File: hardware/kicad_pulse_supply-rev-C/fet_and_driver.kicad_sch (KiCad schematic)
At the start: 52 parts, among them J2 SIG_EXT, Q3 GAN7R0-150LBE, U4 MAX4378, U5 UCC27611DRVT, U6 MCP1703T-5002E/MB

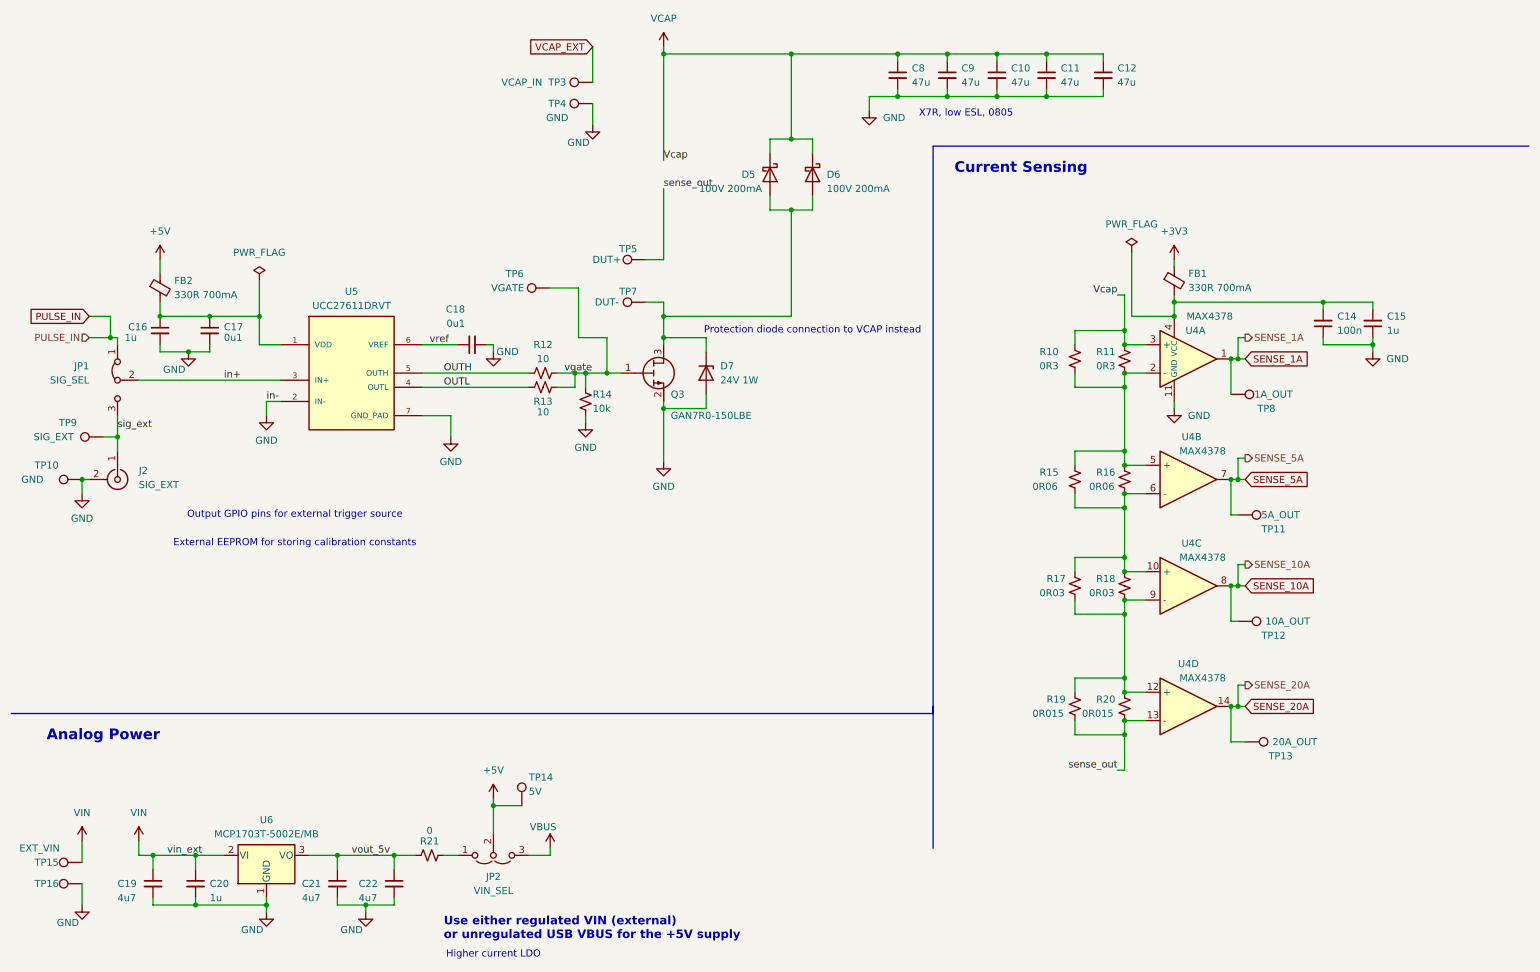
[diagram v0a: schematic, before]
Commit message: hardware breakout boards added, pcb rev-c began
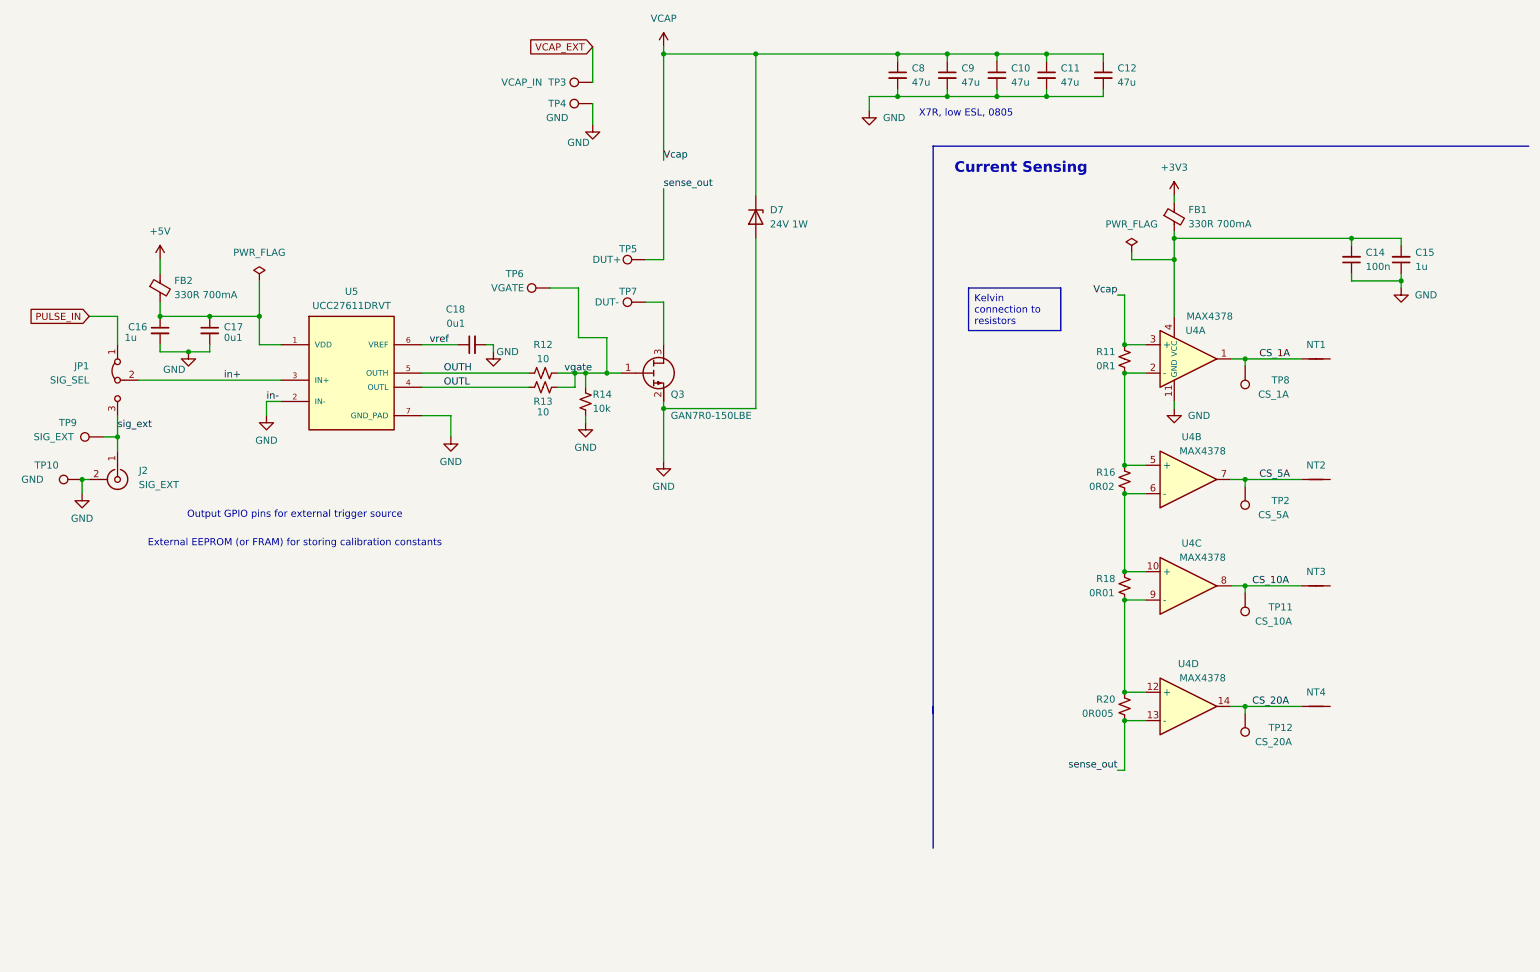
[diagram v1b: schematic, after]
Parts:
- removed C19, C21, C22: 4u7, Capacitor_SMD:C_0805_2012Metric_Pad1.18x1.45mm_HandSolder, symbol Device:C_Small
- removed C20: 1u, Capacitor_SMD:C_0603_1608Metric_Pad1.08x0.95mm_HandSolder, symbol Device:C_Small
- removed D5, D6: 100V 200mA, Diode_SMD:D_SOD-323F, symbol Device:D_Schottky
- removed JP2: VIN_SEL, Connector_PinHeader_2.54mm:PinHeader_1x03_P2.54mm_Vertical, symbol Jumper:Jumper_3_Open
- removed R10: 0R3, Resistor_SMD:R_2010_5025Metric_Pad1.40x2.65mm_HandSolder, symbol Device:R_Small_US
- removed R15: 0R06, Resistor_SMD:R_2010_5025Metric_Pad1.40x2.65mm_HandSolder, symbol Device:R_Small_US
- removed R17: 0R03, Resistor_SMD:R_1206_3216Metric_Pad1.30x1.75mm_HandSolder, symbol Device:R_Small_US
- removed R19: 0R015, Resistor_SMD:R_1206_3216Metric_Pad1.30x1.75mm_HandSolder, symbol Device:R_Small_US
- removed R21: 0, Resistor_SMD:R_0603_1608Metric_Pad0.98x0.95mm_HandSolder, symbol Device:R_Small_US
- removed TP13: 20A_OUT, DW_Library:Keystone-1502-2, symbol Connector:TestPoint
- removed TP14: 5V, DW_Library:Keystone-1502-2, symbol Connector:TestPoint
- removed TP15: EXT_VIN, DW_Library:Keystone-1502-2, symbol Connector:TestPoint
- removed TP16: GND, DW_Library:Keystone-1502-2, symbol Connector:TestPoint
- removed U6: MCP1703T-5002E/MB, Package_TO_SOT_SMD:SOT-89-3, symbol Regulator_Linear:MCP1703Ax-500xxMB
- added NT1, NT2, NT3, NT4: NetTie_2, symbol Device:NetTie_2
- added TP2: CS_5A, DW_Library:Keystone-1502-2, symbol Connector:TestPoint
- R11: value 0R3 -> 0R1; footprint Resistor_SMD:R_2010_5025Metric_Pad1.40x2.65mm_HandSolder -> Resistor_SMD:R_2512_6332Metric
- R16: value 0R06 -> 0R02
- R18: value 0R03 -> 0R01; footprint Resistor_SMD:R_1206_3216Metric_Pad1.30x1.75mm_HandSolder -> Resistor_SMD:R_2512_6332Metric
- R20: value 0R015 -> 0R005; footprint Resistor_SMD:R_1206_3216Metric_Pad1.30x1.75mm_HandSolder -> Resistor_SMD:R_Shunt_Ohmite_LVK25
- TP11: value 5A_OUT -> CS_10A
- TP12: value 10A_OUT -> CS_20A
- TP8: value 1A_OUT -> CS_1A
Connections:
- net VCAP: now also D7.1 (K)
- net at Q3.3 (D), TP7.1: no longer D7.1 (K)
- net SENSE_10A renamed CS_10A
- net CS_10A: now also TP11.1, NT3.1; no longer TP12.1
- net SENSE_1A renamed CS_1A
- net CS_1A: now also NT1.1
- net SENSE_20A renamed CS_20A
- net CS_20A: now also TP12.1, NT4.1
- net SENSE_5A renamed CS_5A
- net CS_5A: now also NT2.1, TP2.1; no longer TP11.1
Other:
- note added: "External EEPROM (or FRAM) for storing calibration constants"
- note removed: "Analog Power"
- note removed: "External EEPROM for storing calibration constants"
- note removed: "Higher current LDO"
- note removed: "Protection diode connection to VCAP instead"
- note removed: "Use either regulated VIN (external) or unregulated USB VBUS for the +5V supply"
- moved on the sheet: C14, C15, D7, FB1, TP8

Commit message: Rev C pcb complete, last commit before branching firmware for new board
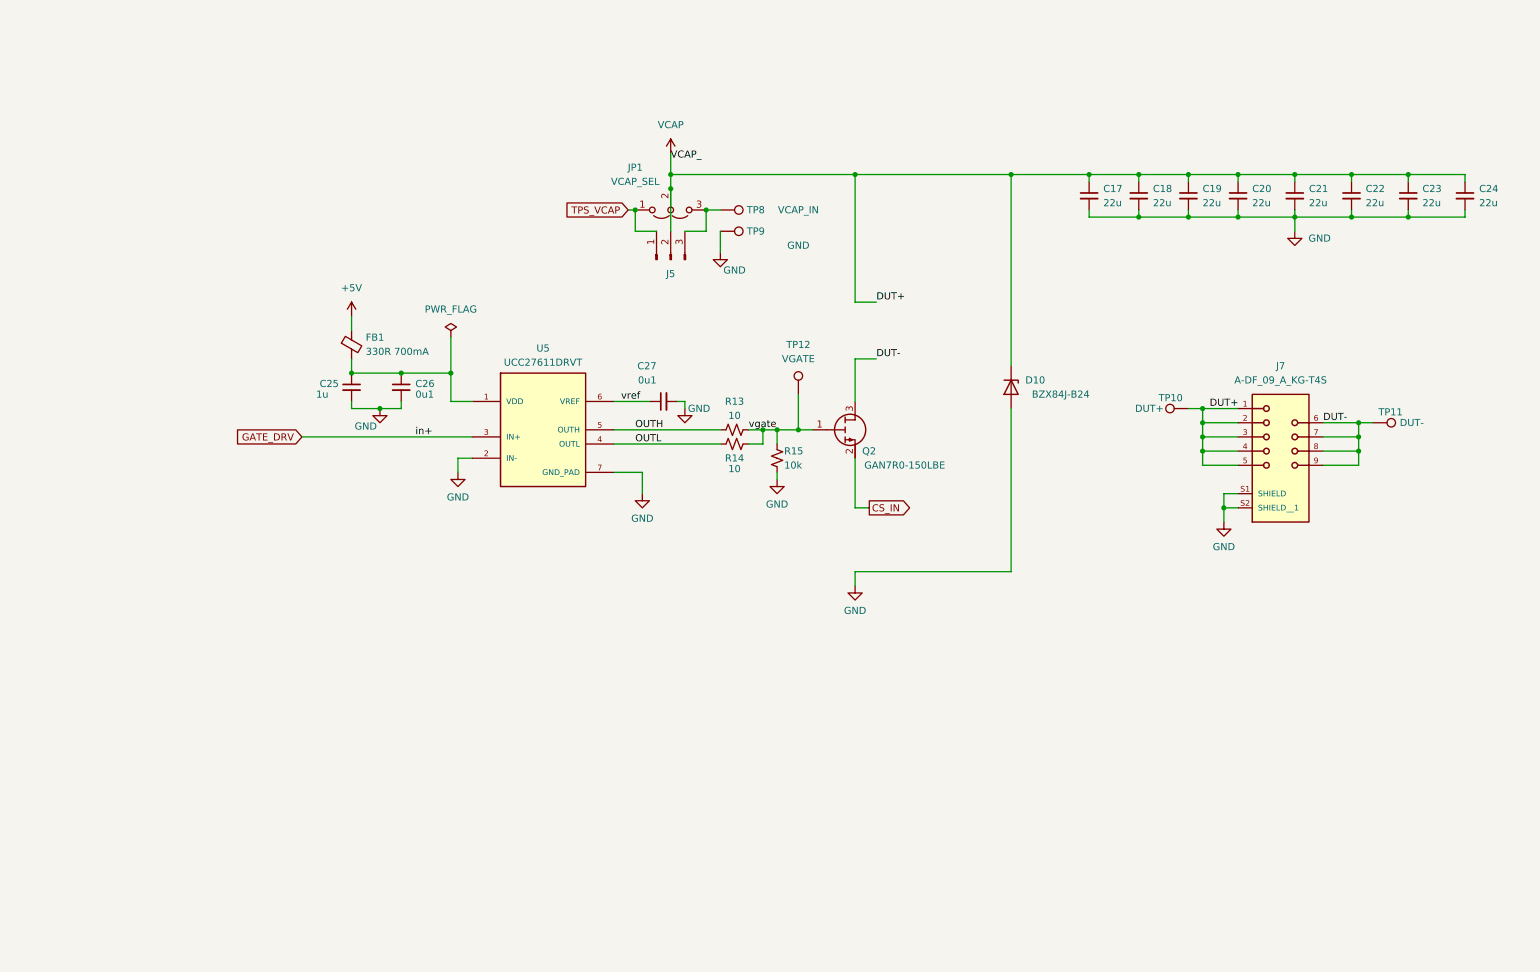
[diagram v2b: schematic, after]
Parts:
- removed C14: 100n, Capacitor_SMD:C_0603_1608Metric_Pad1.08x0.95mm_HandSolder, symbol Device:C_Small
- removed C15: 1u, Capacitor_SMD:C_0603_1608Metric_Pad1.08x0.95mm_HandSolder, symbol Device:C_Small
- removed FB1: 330R 700mA, Capacitor_SMD:C_0402_1005Metric_Pad0.74x0.62mm_HandSolder, symbol Device:FerriteBead_Small
- removed J2: SIG_EXT, DW_Library:BNC_Molex_0731375003, symbol Connector:Conn_Coaxial
- removed JP1: SIG_SEL, Connector_PinHeader_2.54mm:PinHeader_1x03_P2.54mm_Vertical, symbol Jumper:Jumper_3_Bridged12
- removed NT1, NT2, NT3, NT4: NetTie_2, symbol Device:NetTie_2
- removed R11: 0R1, Resistor_SMD:R_2512_6332Metric, symbol Device:R_Small_US
- removed R16: 0R02, Resistor_SMD:R_2010_5025Metric_Pad1.40x2.65mm_HandSolder, symbol Device:R_Small_US
- removed R18: 0R01, Resistor_SMD:R_2512_6332Metric, symbol Device:R_Small_US
- removed R20: 0R005, Resistor_SMD:R_Shunt_Ohmite_LVK25, symbol Device:R_Small_US
- removed TP10: GND, DW_Library:Keystone-1502-2, symbol Connector:TestPoint
- removed TP11: CS_10A, DW_Library:Keystone-1502-2, symbol Connector:TestPoint
- removed TP12: CS_20A, DW_Library:Keystone-1502-2, symbol Connector:TestPoint
- removed TP2: CS_5A, DW_Library:Keystone-1502-2, symbol Connector:TestPoint
- removed TP8: CS_1A, DW_Library:Keystone-1502-2, symbol Connector:TestPoint
- removed TP9: SIG_EXT, DW_Library:Keystone-1502-2, symbol Connector:TestPoint
- removed U4: MAX4378, Package_SO:TSSOP-14_4.4x5mm_P0.65mm, symbol DW_custom_symbols:MAX4378
- added C22, C23, C24: 22u, Capacitor_SMD:C_0805_2012Metric, symbol Device:C_Small
- added J5: Conn_01x03_Pin, Connector_PinHeader_2.54mm:PinHeader_1x03_P2.54mm_Vertical, symbol Connector:Conn_01x03_Pin
- added J7: A-DF_09_A_KG-T4S, DW_Library:ASSMANN_A-DF_09_A_KG-T4S, symbol DW_Library:A-DF_09_A_KG-T4S
- added JP1: VCAP_SEL, DW_Library:custom_jumper, symbol Jumper:Jumper_3_Open
- C17: renamed from C8; value 47u -> 22u; footprint Capacitor_SMD:C_2220_5650Metric -> Capacitor_SMD:C_0805_2012Metric
- C18: renamed from C9; value 47u -> 22u; footprint Capacitor_SMD:C_2220_5650Metric -> Capacitor_SMD:C_0805_2012Metric
- C19: renamed from C10; value 47u -> 22u; footprint Capacitor_SMD:C_2220_5650Metric -> Capacitor_SMD:C_0805_2012Metric
- C20: renamed from C11; value 47u -> 22u; footprint Capacitor_SMD:C_2220_5650Metric -> Capacitor_SMD:C_0805_2012Metric
- C21: renamed from C12; value 47u -> 22u; footprint Capacitor_SMD:C_2220_5650Metric -> Capacitor_SMD:C_0805_2012Metric
- C25: renamed from C16; footprint Capacitor_SMD:C_0603_1608Metric_Pad1.08x0.95mm_HandSolder -> Capacitor_SMD:C_0603_1608Metric
- C26: renamed from C17; footprint Capacitor_SMD:C_0603_1608Metric_Pad1.08x0.95mm_HandSolder -> Capacitor_SMD:C_0603_1608Metric
- C27: renamed from C18; footprint Capacitor_SMD:C_0603_1608Metric_Pad1.08x0.95mm_HandSolder -> Capacitor_SMD:C_0603_1608Metric
- D10: renamed from D7; value 24V 1W -> 24V 550mW; footprint Diode_SMD:D_SMA -> Diode_SMD:D_SOD-323F; MP (none) -> BZX84J-B24
- FB1: renamed from FB2; footprint Capacitor_SMD:C_0402_1005Metric_Pad0.74x0.62mm_HandSolder -> Capacitor_SMD:C_0603_1608Metric
- Q2: renamed from Q3; MP (none) -> GAN7R0-150LBE
- R13: renamed from R12; footprint Resistor_SMD:R_0805_2012Metric_Pad1.20x1.40mm_HandSolder -> Resistor_SMD:R_0603_1608Metric
- R14: renamed from R13; footprint Resistor_SMD:R_0805_2012Metric_Pad1.20x1.40mm_HandSolder -> Resistor_SMD:R_0603_1608Metric
- R15: renamed from R14; footprint Resistor_SMD:R_0603_1608Metric_Pad0.98x0.95mm_HandSolder -> Resistor_SMD:R_0603_1608Metric
- renumbered TP5 to TP10, TP7 to TP11, TP6 to TP12, TP3 to TP8, TP4 to TP9
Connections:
- net sense_out is gone; now on net DUT+: TP10.1
- net GND: now also C22.2, C23.2, C24.2, J7.S1 (SHIELD), J7.S2 (SHIELD__1); no longer Q2.2 (S)
- net  DUT-: now reaches Q2.3 (D), TP11.1
- net  DUT-: now also J7.6, J7.7, J7.8, J7.9
- net VCAP renamed DUT+
- net DUT+: now also C22.1, C23.1, C24.1, J5.2 (Pin_2), J7.1, J7.2, J7.3, J7.4, J7.5, JP1.2 (C)
- net VCAP_EXT: no longer names the net of TP8.1
- net VCAP_EXT: now also J5.3 (Pin_3), JP1.3 (B)
- net in+ renamed GATE_DRV
- new net CS_IN: Q2.2 (S)
- new net TPS_VCAP: J5.1 (Pin_1), JP1.1 (A)
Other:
- note removed: "Current Sensing"
- note removed: "External EEPROM (or FRAM) for storing calibration constants"
- note removed: "Output GPIO pins for external trigger source"
- note removed: "X7R, low ESL, 0805"
- moved on the sheet: C17, C18, C19, C20, C21, C25, C26, C27, D10, FB1, Q2, R13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
